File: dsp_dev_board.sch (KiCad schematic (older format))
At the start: 27 parts, among them J1 9v_jack, J2 aux_mcu_power, J3 input_jack, J7 output_jack, J8 audio_in, J9 audio_out, U1 TL072, U101 TL072, U102 AMS1117-3.3

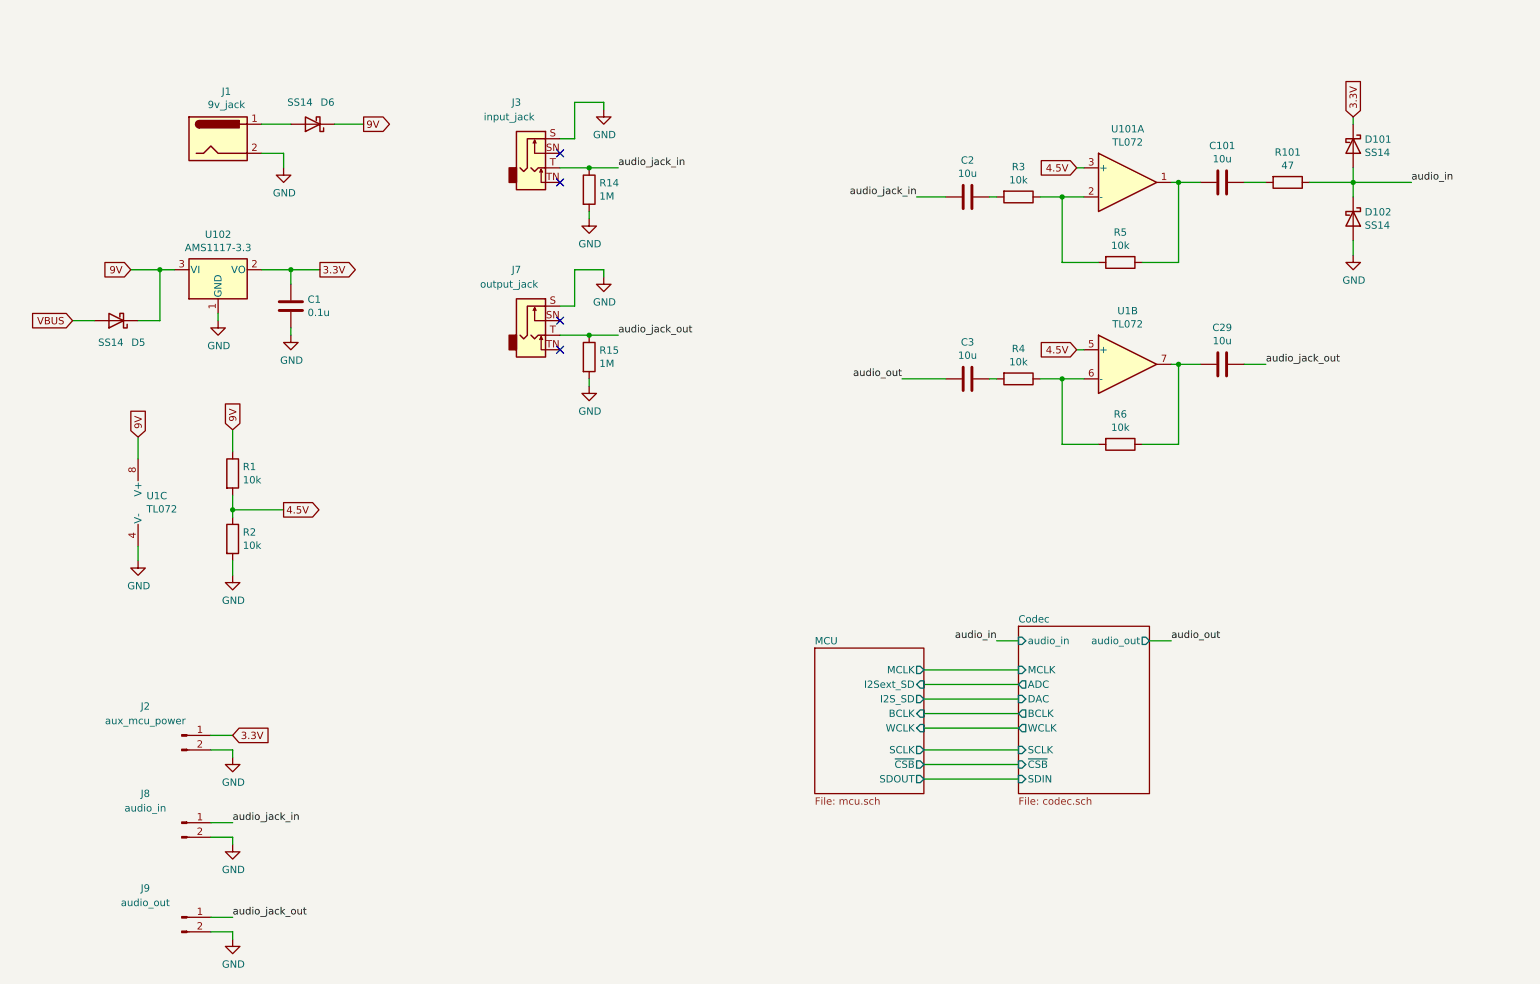
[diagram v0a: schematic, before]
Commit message: Add debug interface
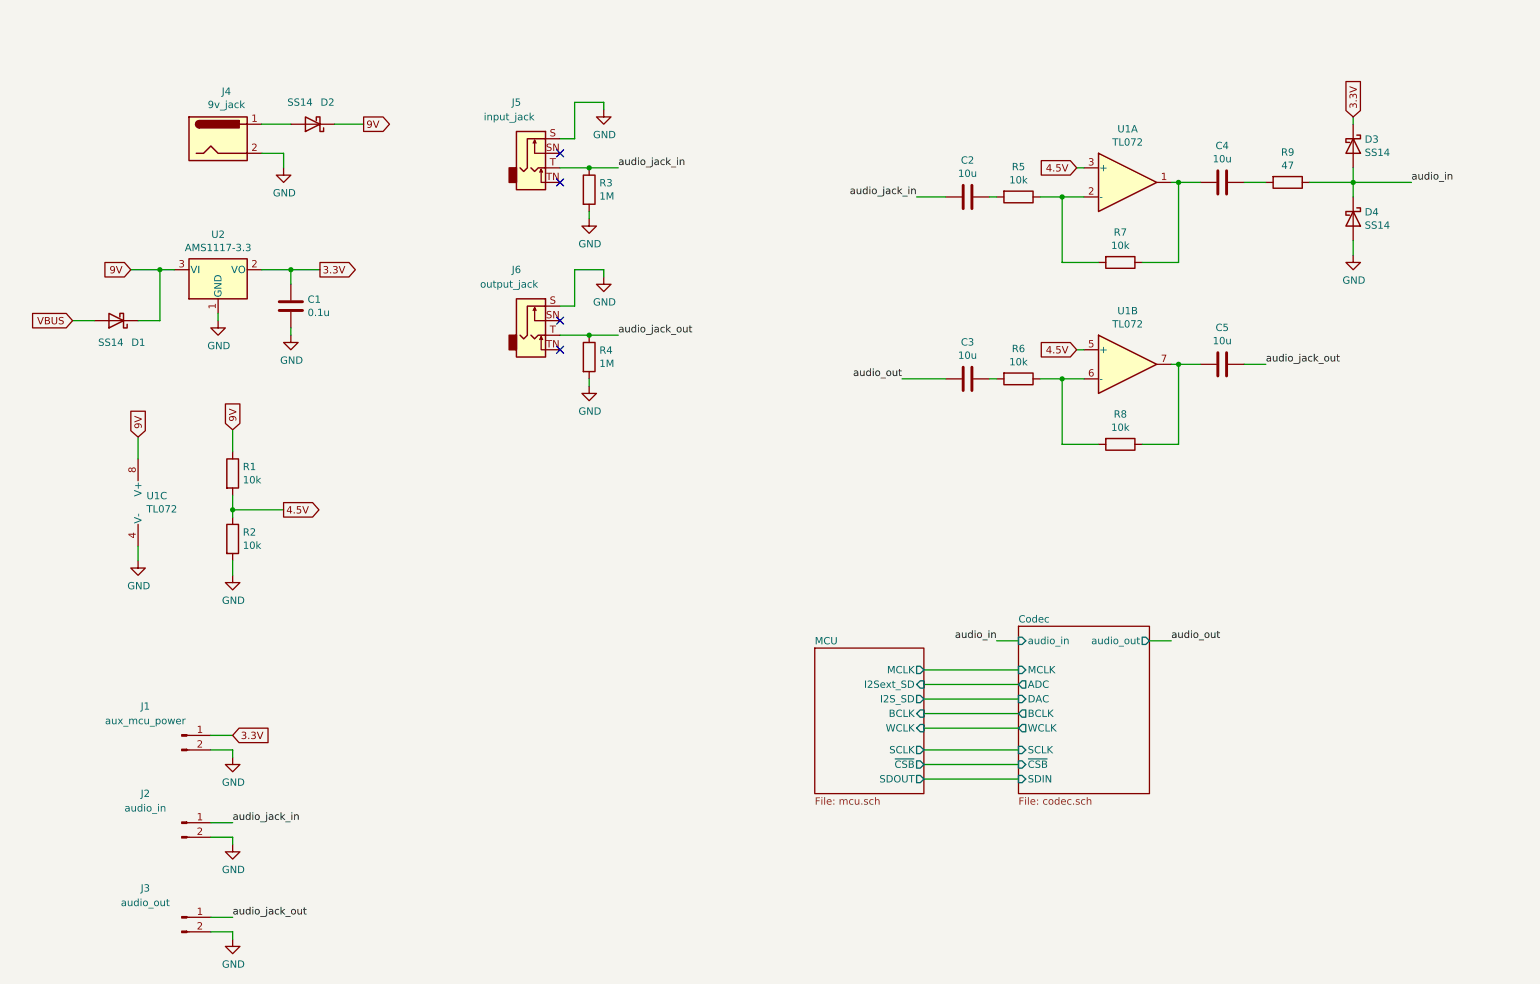
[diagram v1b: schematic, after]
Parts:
- renumbered C101 to C4, C29 to C5, D5 to D1, D6 to D2, D101 to D3, D102 to D4, J2 to J1, J8 to J2, J9 to J3, J1 to J4, J3 to J5, J7 to J6, R14 to R3, R15 to R4, R3 to R5, R4 to R6, R5 to R7, R6 to R8, R101 to R9, U101 to U1, U102 to U2
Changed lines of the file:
@@
 $EndDescr
 $Comp
-L Amplifier_Operational:TL072 U101
+L Amplifier_Operational:TL072 U1
 U 1 1 5FFB8A7E
 P 8300 1800
-F 0 "U101" H 8300 2167 50  0000 C CNN
+F 0 "U1" H 8300 2167 50  0000 C CNN
 F 1 "TL072" H 8300 2076 50  0000 C CNN
 F 2 "" H 8300 1800 50  0001 C CNN
@@
 $EndComp
 $Comp
-L Device:R R101
+L Device:R R9
 U 1 1 5FFBB5A8
 P 9400 1800
-F 0 "R101" V 9193 1800 50  0000 C CNN
+F 0 "R9" V 9193 1800 50  0000 C CNN
 F 1 "47" V 9284 1800 50  0000 C CNN
 F 2 "" V 9330 1800 50  0001 C CNN
@@
 $EndComp
 $Comp
-L power:GND #PWR0101
+L power:GND #PWR013
 U 1 1 5FFBC04C
 P 9850 2300
-F 0 "#PWR0101" H 9850 2050 50  0001 C CNN
+F 0 "#PWR013" H 9850 2050 50  0001 C CNN
 F 1 "GND" H 9855 2127 50  0000 C CNN
 F 2 "" H 9850 2300 50  0001 C CNN
@@
 	9850 2300 9850 2200
 $Comp
-L Device:D_Schottky D102
+L Device:D_Schottky D4
 U 1 1 5FFC1783
 P 9850 2050
-F 0 "D102" V 9804 2129 50  0000 L CNN
+F 0 "D4" V 9804 2129 50  0000 L CNN
 F 1 "SS14" V 9895 2129 50  0000 L CNN
 F 2 "" H 9850 2050 50  0001 C CNN
@@
 	9850 1350 9850 1400
 $Comp
-L Device:D_Schottky D101
+L Device:D_Schottky D3
 U 1 1 5FFC2017
 P 9850 1550
-F 0 "D101" V 9804 1629 50  0000 L CNN
+F 0 "D3" V 9804 1629 50  0000 L CNN
 F 1 "SS14" V 9895 1629 50  0000 L CNN
 F 2 "" H 9850 1550 50  0001 C CNN
@@
 	9850 1800 9850 1900
 $Comp
-L Device:C C101
+L Device:C C4
 U 1 1 5FFCB053
 P 8950 1800
-F 0 "C101" V 8698 1800 50  0000 C CNN
+F 0 "C4" V 8698 1800 50  0000 C CNN
 F 1 "10u" V 8789 1800 50  0000 C CNN
 F 2 "" H 8988 1650 50  0001 C CNN
@@
 	8800 1800 8650 1800
 $Comp
-L Connector:Barrel_Jack J1
+L Connector:Barrel_Jack J4
 U 1 1 60004038
 P 2050 1500
-F 0 "J1" H 2107 1825 50  0000 C CNN
+F 0 "J4" H 2107 1825 50  0000 C CNN
 F 1 "9v_jack" H 2107 1734 50  0000 C CNN
 F 2 "" H 2100 1460 50  0001 C CNN
@@
 9V
 $Comp
-L power:GND #PWR03
+L power:GND #PWR07
 U 1 1 60005258
 P 2500 1700
-F 0 "#PWR03" H 2500 1450 50  0001 C CNN
+F 0 "#PWR07" H 2500 1450 50  0001 C CNN
 F 1 "GND" H 2505 1527 50  0000 C CNN
 F 2 "" H 2500 1700 50  0001 C CNN
@@
 	2500 1600 2350 1600
 $Comp
-L power:GND #PWR05
+L power:GND #PWR011
 U 1 1 6002C64C
 P 4700 1300
-F 0 "#PWR05" H 4700 1050 50  0001 C CNN
+F 0 "#PWR011" H 4700 1050 50  0001 C CNN
 F 1 "GND" H 4705 1127 50  0000 C CNN
 F 2 "" H 4700 1300 50  0001 C CNN
@@
 	7400 4950 7550 4950
 $Comp
-L Device:R R5
+L Device:R R7
 U 1 1 60086C44
 P 8250 2350
-F 0 "R5" V 8043 2350 50  0000 C CNN
+F 0 "R7" V 8043 2350 50  0000 C CNN
 F 1 "10k" V 8134 2350 50  0000 C CNN
 F 2 "" V 8180 2350 50  0001 C CNN
@@
 	2150 3950 2150 4050
 $Comp
-L power:GND #PWR02
+L power:GND #PWR03
 U 1 1 600A2818
 P 2150 4500
-F 0 "#PWR02" H 2150 4250 50  0001 C CNN
+F 0 "#PWR03" H 2150 4250 50  0001 C CNN
 F 1 "GND" H 2155 4327 50  0000 C CNN
 F 2 "" H 2150 4500 50  0001 C CNN
@@
 	8000 1900 7850 1900
 $Comp
-L Device:R R3
+L Device:R R5
 U 1 1 60088EB7
 P 7550 1900
-F 0 "R3" V 7343 1900 50  0000 C CNN
+F 0 "R5" V 7343 1900 50  0000 C CNN
 F 1 "10k" V 7434 1900 50  0000 C CNN
 F 2 "" V 7480 1900 50  0001 C CNN
@@
 	9250 3050 9100 3050
 $Comp
-L Device:R R6
+L Device:R R8
 U 1 1 600B8877
 P 8250 3600
-F 0 "R6" V 8043 3600 50  0000 C CNN
+F 0 "R8" V 8043 3600 50  0000 C CNN
 F 1 "10k" V 8134 3600 50  0000 C CNN
 F 2 "" V 8180 3600 50  0001 C CNN
@@
 	8000 3150 7850 3150
 $Comp
-L Device:R R4
+L Device:R R6
 U 1 1 600B888A
 P 7550 3150
-F 0 "R4" V 7343 3150 50  0000 C CNN
+F 0 "R6" V 7343 3150 50  0000 C CNN
 F 1 "10k" V 7434 3150 50  0000 C CNN
 F 2 "" V 7480 3150 50  0001 C CNN
@@
 	6900 5700 7550 5700
 $Comp
-L Device:C C29
+L Device:C C5
 U 1 1 600DC113
 P 8950 3050
-F 0 "C29" V 8698 3050 50  0000 C CNN
+F 0 "C5" V 8698 3050 50  0000 C CNN
 F 1 "10u" V 8789 3050 50  0000 C CNN
 F 2 "" H 8988 2900 50  0001 C CNN
@@
 NoConn ~ 4400 1600
 $Comp
-L power:GND #PWR020
+L power:GND #PWR012
 U 1 1 601D9CA8
 P 4700 2450
-F 0 "#PWR020" H 4700 2200 50  0001 C CNN
+F 0 "#PWR012" H 4700 2200 50  0001 C CNN
 F 1 "GND" H 4705 2277 50  0000 C CNN
 F 2 "" H 4700 2450 50  0001 C CNN
@@
 NoConn ~ 4400 2750
 $Comp
-L Connector:AudioJack2_Switch J7
+L Connector:AudioJack2_Switch J6
 U 1 1 601D9CB6
 P 4200 2850
-F 0 "J7" H 4100 3300 50  0000 C CNN
+F 0 "J6" H 4100 3300 50  0000 C CNN
 F 1 "output_jack" H 4050 3200 50  0000 C CNN
 F 2 "Connector_Audio:Jack_6.35mm_Neutrik_NMJ4HCD2_Horizontal" H 4200 3050 50  0001 C CNN
@@
 	2550 2850 2550 2800
 $Comp
-L power:GND #PWR04
+L power:GND #PWR08
 U 1 1 60006D77
 P 2550 2850
-F 0 "#PWR04" H 2550 2600 50  0001 C CNN
+F 0 "#PWR08" H 2550 2600 50  0001 C CNN
 F 1 "GND" H 2555 2677 50  0000 C CNN
 F 2 "" H 2550 2850 50  0001 C CNN
@@
 	2050 2750 2050 2700
 $Comp
-L power:GND #PWR0103
+L power:GND #PWR02
 U 1 1 5FFC34F5
 P 2050 2750
-F 0 "#PWR0103" H 2050 2500 50  0001 C CNN
+F 0 "#PWR02" H 2050 2500 50  0001 C CNN
 F 1 "GND" H 2055 2577 50  0000 C CNN
 F 2 "" H 2050 2750 50  0001 C CNN
@@
 $EndComp
 $Comp
-L Regulator_Linear:AMS1117-3.3 U102
+L Regulator_Linear:AMS1117-3.3 U2
 U 1 1 5FFC29B1
 P 2050 2400
-F 0 "U102" H 2050 2642 50  0000 C CNN
+F 0 "U2" H 2050 2642 50  0000 C CNN
 F 1 "AMS1117-3.3" H 2050 2551 50  0000 C CNN
 F 2 "Package_TO_SOT_SMD:SOT-223-3_TabPin2" H 2050 2600 50  0001 C CNN
@@
 $EndComp
 $Comp
-L Connector:Conn_01x02_Male J2
+L Connector:Conn_01x02_Male J1
 U 1 1 601E5519
 P 1800 5600
-F 0 "J2" H 1550 5800 50  0000 C CNN
+F 0 "J1" H 1550 5800 50  0000 C CNN
 F 1 "aux_mcu_power" H 1550 5700 50  0000 C CNN
 F 2 "" H 1800 5600 50  0001 C CNN
@@
 3.3V
 $Comp
-L power:GND #PWR06
+L power:GND #PWR04
 U 1 1 601E6A36
 P 2150 5750
-F 0 "#PWR06" H 2150 5500 50  0001 C CNN
+F 0 "#PWR04" H 2150 5500 50  0001 C CNN
 F 1 "GND" H 2155 5577 50  0000 C CNN
 F 2 "" H 2150 5750 50  0001 C CNN
@@
 audio_jack_out
 $Comp
-L Connector:Conn_01x02_Male J8
+L Connector:Conn_01x02_Male J2
 U 1 1 6026815E
 P 1800 6200
-F 0 "J8" H 1550 6400 50  0000 C CNN
+F 0 "J2" H 1550 6400 50  0000 C CNN
 F 1 "audio_in" H 1550 6300 50  0000 C CNN
 F 2 "" H 1800 6200 50  0001 C CNN
@@
 $EndComp
 $Comp
-L power:GND #PWR021
+L power:GND #PWR05
 U 1 1 6026A61A
 P 2150 6350
-F 0 "#PWR021" H 2150 6100 50  0001 C CNN
+F 0 "#PWR05" H 2150 6100 50  0001 C CNN
 F 1 "GND" H 2155 6177 50  0000 C CNN
 F 2 "" H 2150 6350 50  0001 C CNN
@@
 	2150 6850 2000 6850
 $Comp
-L Connector:Conn_01x02_Male J9
+L Connector:Conn_01x02_Male J3
 U 1 1 60272181
 P 1800 6850
-F 0 "J9" H 1550 7050 50  0000 C CNN
+F 0 "J3" H 1550 7050 50  0000 C CNN
 F 1 "audio_out" H 1550 6950 50  0000 C CNN
 F 2 "" H 1800 6850 50  0001 C CNN
@@
 $EndComp
 $Comp
-L power:GND #PWR026
+L power:GND #PWR06
 U 1 1 60272187
 P 2150 7000
-F 0 "#PWR026" H 2150 6750 50  0001 C CNN
+F 0 "#PWR06" H 2150 6750 50  0001 C CNN
 F 1 "GND" H 2155 6827 50  0000 C CNN
 F 2 "" H 2150 7000 50  0001 C CNN
@@
 	2150 6950 2000 6950
 $Comp
-L Device:D_Schottky D5
+L Device:D_Schottky D1
 U 1 1 6020CE2E
 P 1350 2750
-F 0 "D5" H 1150 2900 50  0000 L CNN
+F 0 "D1" H 1150 2900 50  0000 L CNN
 F 1 "SS14" H 1300 2900 50  0000 L CNN
 F 2 "" H 1350 2750 50  0001 C CNN
@@
 	1200 2750 1050 2750
 $Comp
-L Connector:AudioJack2_Switch J3
+L Connector:AudioJack2_Switch J5
 U 1 1 601CE4FA
 P 4200 1700
-F 0 "J3" H 4100 2150 50  0000 C CNN
+F 0 "J5" H 4100 2150 50  0000 C CNN
 F 1 "input_jack" H 4050 2050 50  0000 C CNN
 F 2 "Connector_Audio:Jack_6.35mm_Neutrik_NMJ4HCD2_Horizontal" H 4200 1900 50  0001 C CNN
@@
 $EndComp
 $Comp
-L Device:R R14
+L Device:R R3
 U 1 1 600E7C35
 P 4600 1850
-F 0 "R14" H 4670 1896 50  0000 L CNN
+F 0 "R3" H 4670 1896 50  0000 L CNN
 F 1 "1M" H 4670 1805 50  0000 L CNN
 F 2 "" V 4530 1850 50  0001 C CNN
@@
 $EndComp
 $Comp
-L power:GND #PWR033
+L power:GND #PWR09
 U 1 1 600E8A0A
 P 4600 2050
-F 0 "#PWR033" H 4600 1800 50  0001 C CNN
+F 0 "#PWR09" H 4600 1800 50  0001 C CNN
 F 1 "GND" H 4605 1877 50  0000 C CNN
 F 2 "" H 4600 2050 50  0001 C CNN
@@
 	4600 2050 4600 2000
 $Comp
-L Device:R R15
+L Device:R R4
 U 1 1 600EC6BA
 P 4600 3000
-F 0 "R15" H 4670 3046 50  0000 L CNN
+F 0 "R4" H 4670 3046 50  0000 L CNN
 F 1 "1M" H 4670 2955 50  0000 L CNN
 F 2 "" V 4530 3000 50  0001 C CNN
@@
 $EndComp
 $Comp
-L power:GND #PWR034
+L power:GND #PWR010
 U 1 1 600EC6C0
 P 4600 3200
-F 0 "#PWR034" H 4600 2950 50  0001 C CNN
+F 0 "#PWR010" H 4600 2950 50  0001 C CNN
 F 1 "GND" H 4605 3027 50  0000 C CNN
 F 2 "" H 4600 3200 50  0001 C CNN
@@
 Connection ~ 4600 1700
 $Comp
-L Device:D_Schottky D6
+L Device:D_Schottky D2
 U 1 1 60286E4B
 P 2700 1400
-F 0 "D6" H 2550 1250 50  0000 L CNN
+F 0 "D2" H 2550 1250 50  0000 L CNN
 F 1 "SS14" H 2700 1250 50  0000 L CNN
 F 2 "" H 2700 1400 50  0001 C CNN

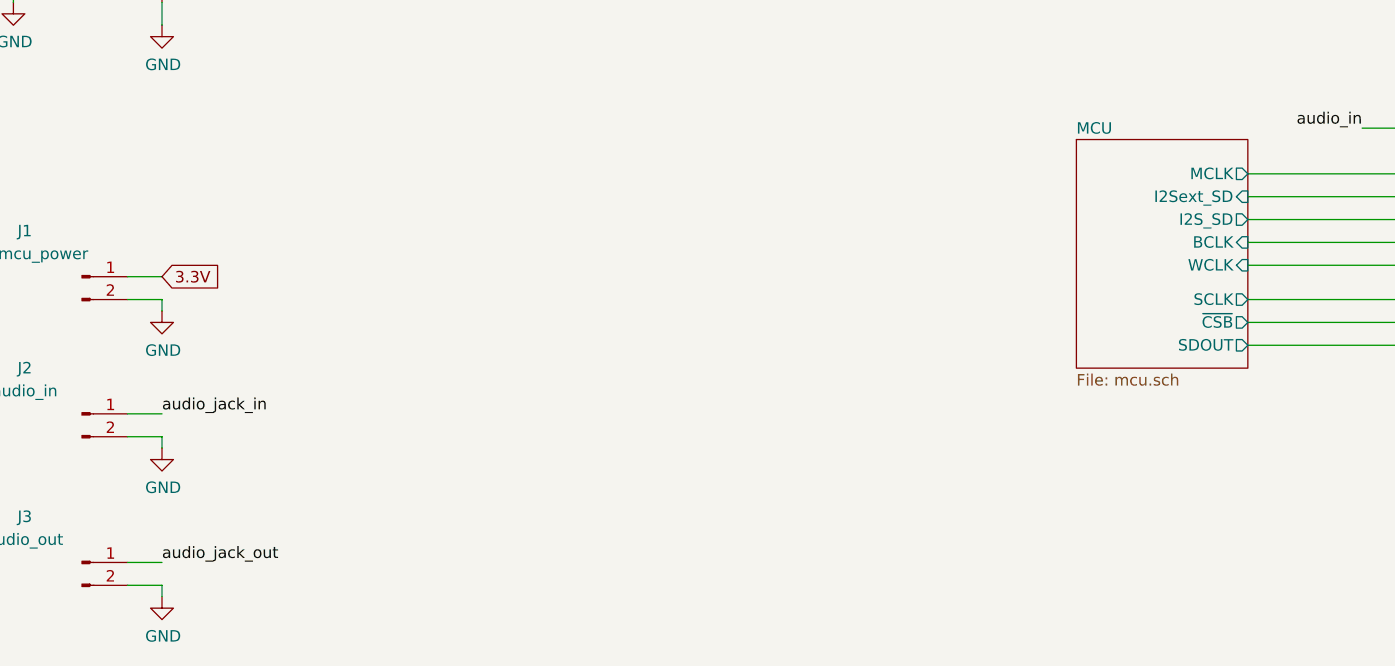
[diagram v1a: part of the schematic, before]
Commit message: Add traces
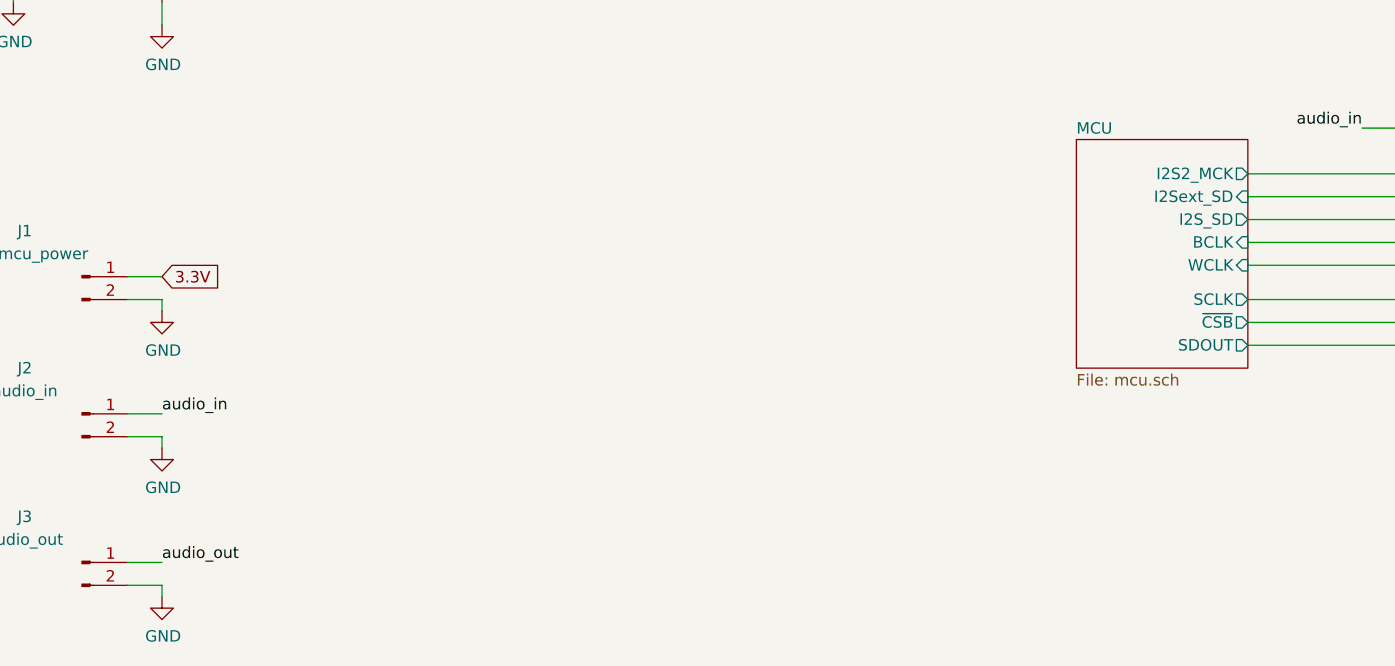
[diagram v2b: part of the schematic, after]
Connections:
- net audio_in: now also J2.1 (Pin_1)
- net audio_jack_in: no longer J2.1 (Pin_1)
- net audio_jack_out: no longer J3.1 (Pin_1)
- net audio_out: now also J3.1 (Pin_1)
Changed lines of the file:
@@
 F0 "MCU" 50
 F1 "mcu.sch" 50
-F2 "MCLK" O R 6900 5150 50
-F3 "BCLK" I R 6900 5450 50
-F4 "WCLK" I R 6900 5550 50
-F5 "I2S_SD" O R 6900 5350 50
-F6 "I2Sext_SD" I R 6900 5250 50
-F7 "SCLK" O R 6900 5700 50
-F8 "~CSB" O R 6900 5800 50
-F9 "SDOUT" O R 6900 5900 50
+F2 "BCLK" I R 6900 5450 50
+F3 "WCLK" I R 6900 5550 50
+F4 "I2S_SD" O R 6900 5350 50
+F5 "I2Sext_SD" I R 6900 5250 50
+F6 "SCLK" O R 6900 5700 50
+F7 "~CSB" O R 6900 5800 50
+F8 "SDOUT" O R 6900 5900 50
+F9 "I2S2_MCK" O R 6900 5150 50
 $EndSheet
 Text Label 10250 1800 0    50   ~ 0
@@
 	2000 5600 2150 5600
 Text Label 2150 6200 0    50   ~ 0
-audio_jack_in
+audio_in
 Wire Wire Line
 	2150 6200 2000 6200
 Text Label 2150 6850 0    50   ~ 0
-audio_jack_out
+audio_out
 $Comp
 L Connector:Conn_01x02_Male J2
